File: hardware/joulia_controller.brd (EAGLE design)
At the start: 121 x 68 mm, 41 parts, among them IC1 LM2902D, IC2 LM2902D, U1 MMBT2222ALT1G, U2 MMBT2222ALT1G

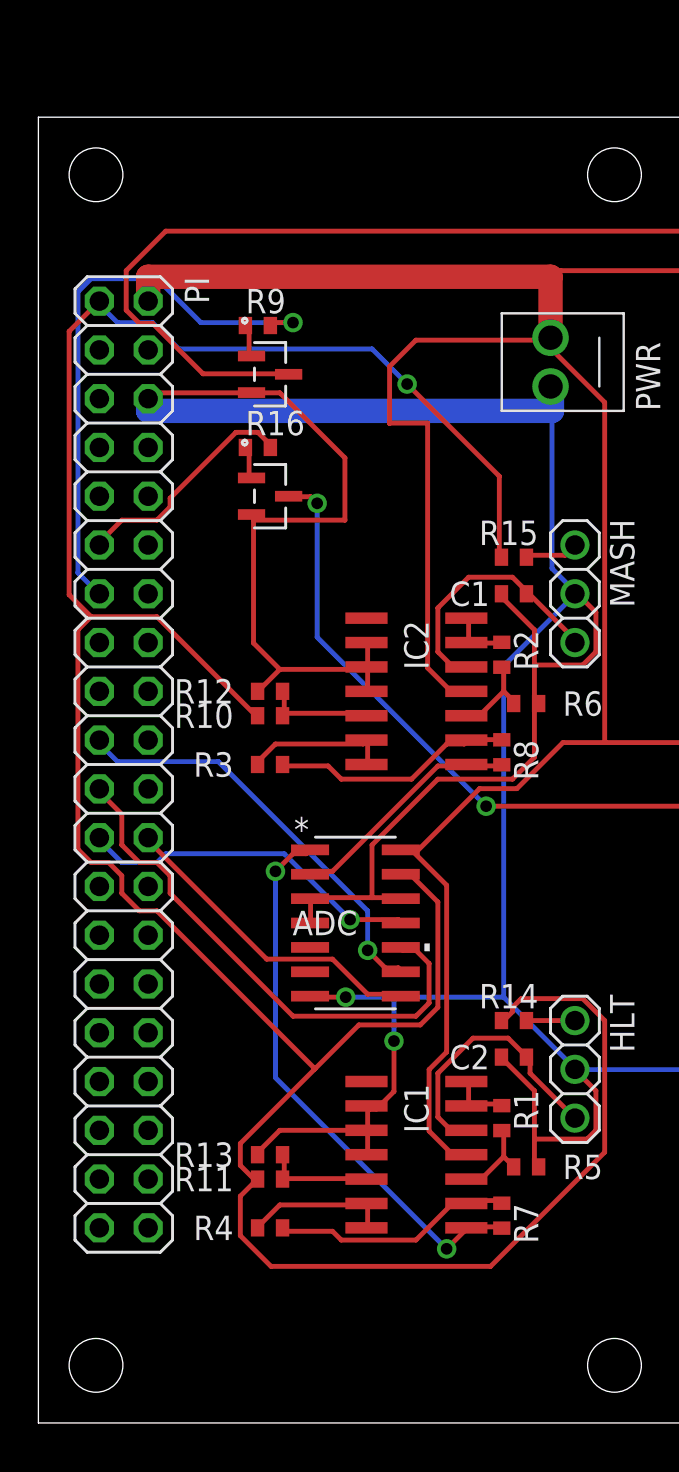
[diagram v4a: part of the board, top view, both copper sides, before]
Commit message: Adding LEDs and Fan Connector
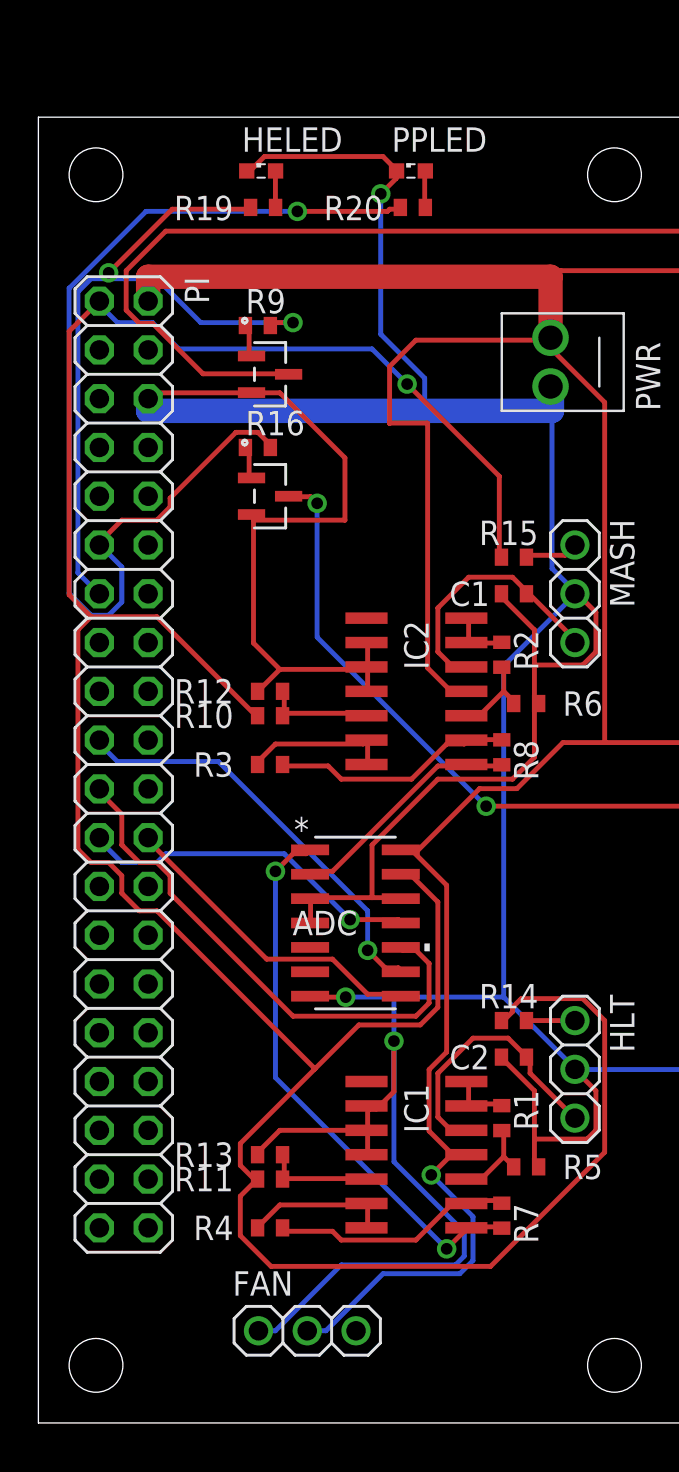
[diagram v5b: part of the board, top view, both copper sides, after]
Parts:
- added FAN: (no value), adafruit:1X03
- added HELED, PPLED: (no value), eagle-ltspice:LED_SML0603
- added R19, R20: 220, rcl:R0402
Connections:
- new net N$25: HELED.A, R19.2
- new net N$26: PPLED.A, R20.2
- net +5V: now also FAN.2
- net GND: now also FAN.1, HELED.C, PPLED.C
- net HEOUT: now also R19.1
- net PPOUT: now also R20.1
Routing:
- net GND: track 368.1 -> 415.4 mm, vias 2 -> 3
- net PPOUT: track 12.1 -> 54.0 mm, vias 0 -> 1
- net +5V: track 150.0 -> 167.7 mm, vias 0 -> 1
- net HEOUT: track 29.9 -> 39.0 mm, vias 1 -> 2
- net N$26: track 0.00 -> 1.93 mm
- net N$25: track 0.00 -> 1.90 mm
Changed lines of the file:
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@@
 <attribute name="NAME" x="37.53" y="33.07" size="1.27" layer="25" align="bottom-right"/>
 </element>
+<element name="HELED" library="eagle-ltspice" library_urn="urn:adsk.eagle:library:217" package="LED_SML0603" value="" x="11.6" y="65.2">
+<attribute name="SPICEMODEL" value="NONE" x="11.6" y="65.2" size="1.778" layer="27" display="off"/>
+<attribute name="SPICEPREFIX" value="D" x="11.6" y="65.2" size="1.778" layer="27" display="off"/>
+<attribute name="SPICETYPE" value="diode" x="11.6" y="65.2" size="1.778" layer="27" display="off"/>
+</element>
+<element name="PPLED" library="eagle-ltspice" library_urn="urn:adsk.eagle:library:217" package="LED_SML0603" value="" x="19.4" y="65.2">
+<attribute name="SPICEMODEL" value="NONE" x="19.4" y="65.2" size="1.778" layer="27" display="off"/>
+<attribute name="SPICEPREFIX" value="D" x="19.4" y="65.2" size="1.778" layer="27" display="off"/>
+<attribute name="SPICETYPE" value="diode" x="19.4" y="65.2" size="1.778" layer="27" display="off"/>
+</element>
+<element name="R19" library="rcl" library_urn="urn:adsk.eagle:library:334" package="R0402" value="220" x="11.7" y="63.3" smashed="yes">
+<attribute name="NAME" x="7.065" y="62.635" size="1.27" layer="25"/>
+</element>
+<element name="R20" library="rcl" library_urn="urn:adsk.eagle:library:334" package="R0402" value="220" x="19.5" y="63.3" smashed="yes">
+<attribute name="NAME" x="14.865" y="62.635" size="1.27" layer="25"/>
+</element>
+<element name="FAN" library="adafruit" package="1X03" value="" x="14" y="4.8"/>
 </elements>
 <signals>
@@
 <wire x1="26.67" y1="53.975" x2="26.7462" y2="53.975" width="1.27" layer="16"/>
 <wire x1="26.7462" y1="53.975" x2="26.7462" y2="52.705" width="1.27" layer="16"/>
-<wire x1="26.7462" y1="52.705" x2="5.715" y2="52.705" width="1.27" layer="16"/>
+<wire x1="26.7462" y1="52.705" x2="20.1168" y2="52.705" width="1.27" layer="16"/>
+<wire x1="20.1168" y1="52.705" x2="5.715" y2="52.705" width="1.27" layer="16"/>
 <wire x1="5.715" y1="52.705" x2="5.715" y2="53.34" width="1.27" layer="16"/>
 <wire x1="15.9639" y1="47.0154" x2="15.9639" y2="50.2539" width="0.254" layer="1"/>
@@
 <wire x1="113.5" y1="39.1" x2="113.5" y2="15.202" width="0.254" layer="1"/>
 <wire x1="113.5" y1="15.202" x2="108.2421" y2="10.8441" width="0.254" layer="1"/>
+<contactref element="HELED" pad="C"/>
+<contactref element="PPLED" pad="C"/>
+<wire x1="11.0871" y1="65.2653" x2="10.8585" y2="65.2653" width="0.254" layer="1"/>
+<wire x1="11.7729" y1="65.9511" x2="11.0871" y2="65.2653" width="0.254" layer="1"/>
+<wire x1="17.9451" y1="65.9511" x2="11.7729" y2="65.9511" width="0.254" layer="1"/>
+<wire x1="18.6309" y1="65.2653" x2="17.9451" y2="65.9511" width="0.254" layer="1"/>
+<wire x1="10.8585" y1="65.2653" x2="10.85" y2="65.2" width="0.254" layer="1"/>
+<wire x1="18.6309" y1="65.2653" x2="18.65" y2="65.2" width="0.254" layer="1"/>
+<wire x1="18.6309" y1="64.8081" x2="18.6309" y2="65.151" width="0.254" layer="1"/>
+<wire x1="17.8308" y1="64.008" x2="18.6309" y2="64.8081" width="0.254" layer="1"/>
+<wire x1="17.8308" y1="56.6928" x2="17.8308" y2="64.008" width="0.254" layer="16"/>
+<wire x1="20.1168" y1="54.4068" x2="17.8308" y2="56.6928" width="0.254" layer="16"/>
+<wire x1="20.1168" y1="52.705" x2="20.1168" y2="54.4068" width="0.254" layer="16"/>
+<wire x1="18.6309" y1="65.151" x2="18.65" y2="65.2" width="0.254" layer="1"/>
+<via x="17.8308" y="64.008" extent="1-16" drill="0.6096"/>
+<contactref element="FAN" pad="1"/>
+<wire x1="12.3444" y1="4.8006" x2="11.5443" y2="4.8006" width="0.254" layer="16"/>
+<wire x1="15.7734" y1="8.2296" x2="12.3444" y2="4.8006" width="0.254" layer="16"/>
+<wire x1="21.717" y1="8.2296" x2="15.7734" y2="8.2296" width="0.254" layer="16"/>
+<wire x1="22.1742" y1="8.6868" x2="21.717" y2="8.2296" width="0.254" layer="16"/>
+<wire x1="22.1742" y1="9.9441" x2="22.1742" y2="8.6868" width="0.254" layer="16"/>
+<wire x1="18.5166" y1="13.6017" x2="22.1742" y2="9.9441" width="0.254" layer="16"/>
+<wire x1="18.5166" y1="19.8882" x2="18.5166" y2="13.6017" width="0.254" layer="16"/>
+<wire x1="11.5443" y1="4.8006" x2="11.46" y2="4.8" width="0.254" layer="16"/>
 </signal>
 <signal name="N$4">
@@
 <wire x1="29.4894" y1="35.433" x2="29.4894" y2="53.1495" width="0.254" layer="1"/>
 <wire x1="26.7462" y1="55.8927" x2="26.67" y2="56.515" width="0.254" layer="1"/>
+<contactref element="FAN" pad="2"/>
+<wire x1="14.9733" y1="4.8006" x2="14.0589" y2="4.8006" width="0.254" layer="16"/>
+<wire x1="17.9451" y1="7.7724" x2="14.9733" y2="4.8006" width="0.254" layer="16"/>
+<wire x1="21.9456" y1="7.7724" x2="17.9451" y2="7.7724" width="0.254" layer="16"/>
+<wire x1="22.6314" y1="8.4582" x2="21.9456" y2="7.7724" width="0.254" layer="16"/>
+<wire x1="22.6314" y1="10.7442" x2="22.6314" y2="8.4582" width="0.254" layer="16"/>
+<wire x1="20.4597" y1="12.9159" x2="22.6314" y2="10.7442" width="0.254" layer="16"/>
+<wire x1="21.4884" y1="13.9446" x2="20.4597" y2="12.9159" width="0.254" layer="1"/>
+<wire x1="14.0589" y1="4.8006" x2="14" y2="4.8" width="0.254" layer="16"/>
+<wire x1="21.4884" y1="13.9446" x2="22.285" y2="13.97" width="0.254" layer="1"/>
+<via x="20.4597" y="12.9159" extent="1-16" drill="0.6096"/>
 </signal>
 <signal name="+3V3">
@@
 <wire x1="8.4582" y1="57.3024" x2="13.2588" y2="57.3024" width="0.254" layer="16"/>
 <wire x1="6.1722" y1="59.5884" x2="8.4582" y2="57.3024" width="0.254" layer="16"/>
-<wire x1="2.7432" y1="59.5884" x2="6.1722" y2="59.5884" width="0.254" layer="16"/>
+<wire x1="2.7432" y1="59.5884" x2="3.6576" y2="59.5884" width="0.254" layer="16"/>
+<wire x1="3.6576" y1="59.5884" x2="6.1722" y2="59.5884" width="0.254" layer="16"/>
 <wire x1="2.0574" y1="58.9026" x2="2.7432" y2="59.5884" width="0.254" layer="16"/>
 <wire x1="2.0574" y1="44.2722" x2="2.0574" y2="58.9026" width="0.254" layer="16"/>
@@
 <wire x1="2.9718" y1="43.3578" x2="3.175" y2="43.18" width="0.254" layer="16"/>
 <via x="13.2588" y="57.3024" extent="1-16" drill="0.6096"/>
+<contactref element="R19" pad="1"/>
+<wire x1="6.9723" y1="63.2079" x2="10.9728" y2="63.2079" width="0.254" layer="1"/>
+<wire x1="3.6576" y1="59.8932" x2="6.9723" y2="63.2079" width="0.254" layer="1"/>
+<wire x1="3.6576" y1="59.5884" x2="3.6576" y2="59.8932" width="0.254" layer="16"/>
+<wire x1="10.9728" y1="63.2079" x2="11.05" y2="63.3" width="0.254" layer="1"/>
+<via x="3.6576" y="59.8932" extent="1-16" drill="0.6096"/>
 </signal>
 <signal name="PPOUT">
@@
 <wire x1="11.8872" y1="50.9016" x2="12.08" y2="50.8" width="0.254" layer="1"/>
 <wire x1="3.2004" y1="45.8724" x2="3.175" y2="45.72" width="0.254" layer="1"/>
+<contactref element="R20" pad="1"/>
+<wire x1="18.288" y1="63.2079" x2="18.7452" y2="63.2079" width="0.254" layer="1"/>
+<wire x1="18.1737" y1="63.0936" x2="18.288" y2="63.2079" width="0.254" layer="1"/>
+<wire x1="13.4874" y1="63.0936" x2="18.1737" y2="63.0936" width="0.254" layer="1"/>
+<wire x1="5.6007" y1="63.0936" x2="13.4874" y2="63.0936" width="0.254" layer="16"/>
+<wire x1="1.6002" y1="59.0931" x2="5.6007" y2="63.0936" width="0.254" layer="16"/>
+<wire x1="1.6002" y1="43.2054" x2="1.6002" y2="59.0931" width="0.254" layer="16"/>
+<wire x1="2.7432" y1="42.0624" x2="1.6002" y2="43.2054" width="0.254" layer="16"/>
+<wire x1="3.6576" y1="42.0624" x2="2.7432" y2="42.0624" width="0.254" layer="16"/>
+<wire x1="4.3434" y1="42.7482" x2="3.6576" y2="42.0624" width="0.254" layer="16"/>
+<wire x1="4.3434" y1="44.577" x2="4.3434" y2="42.7482" width="0.254" layer="16"/>
+<wire x1="3.2004" y1="45.72" x2="4.3434" y2="44.577" width="0.254" layer="16"/>
+<wire x1="18.7452" y1="63.2079" x2="18.85" y2="63.3" width="0.254" layer="1"/>
+<wire x1="3.2004" y1="45.72" x2="3.175" y2="45.72" width="0.254" layer="16"/>
+<via x="13.4874" y="63.0936" extent="1-16" drill="0.6096"/>
 </signal>
 <signal name="N$15">
@@
 <wire x1="100.6983" y1="16.002" x2="100.665" y2="16.3" width="0.762" layer="1"/>
 </signal>
+<signal name="N$25">
+<contactref element="HELED" pad="A"/>
+<contactref element="R19" pad="2"/>
+<wire x1="12.3444" y1="63.3222" x2="12.3444" y2="65.151" width="0.254" layer="1"/>
+<wire x1="12.3444" y1="65.151" x2="12.35" y2="65.2" width="0.254" layer="1"/>
+<wire x1="12.3444" y1="63.3222" x2="12.35" y2="63.3" width="0.254" layer="1"/>
+</signal>
+<signal name="N$26">
+<contactref element="R20" pad="2"/>
+<contactref element="PPLED" pad="A"/>
+<wire x1="20.1168" y1="63.3222" x2="20.1168" y2="65.151" width="0.254" layer="1"/>
+<wire x1="20.1168" y1="65.151" x2="20.15" y2="65.2" width="0.254" layer="1"/>
+<wire x1="20.1168" y1="63.3222" x2="20.15" y2="63.3" width="0.254" layer="1"/>
+</signal>
 </signals>

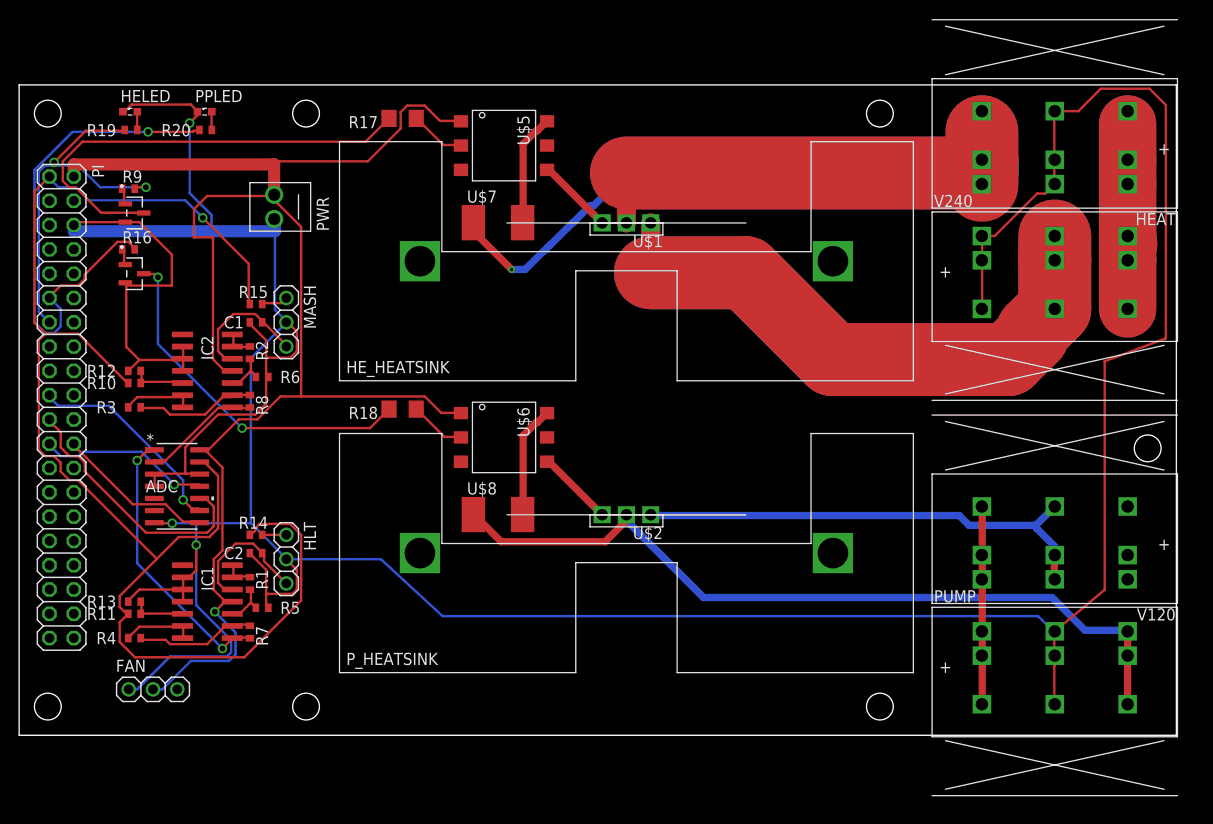
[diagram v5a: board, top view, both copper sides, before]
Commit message: Switching to mechanical relay for pump and horizontal heatsink.
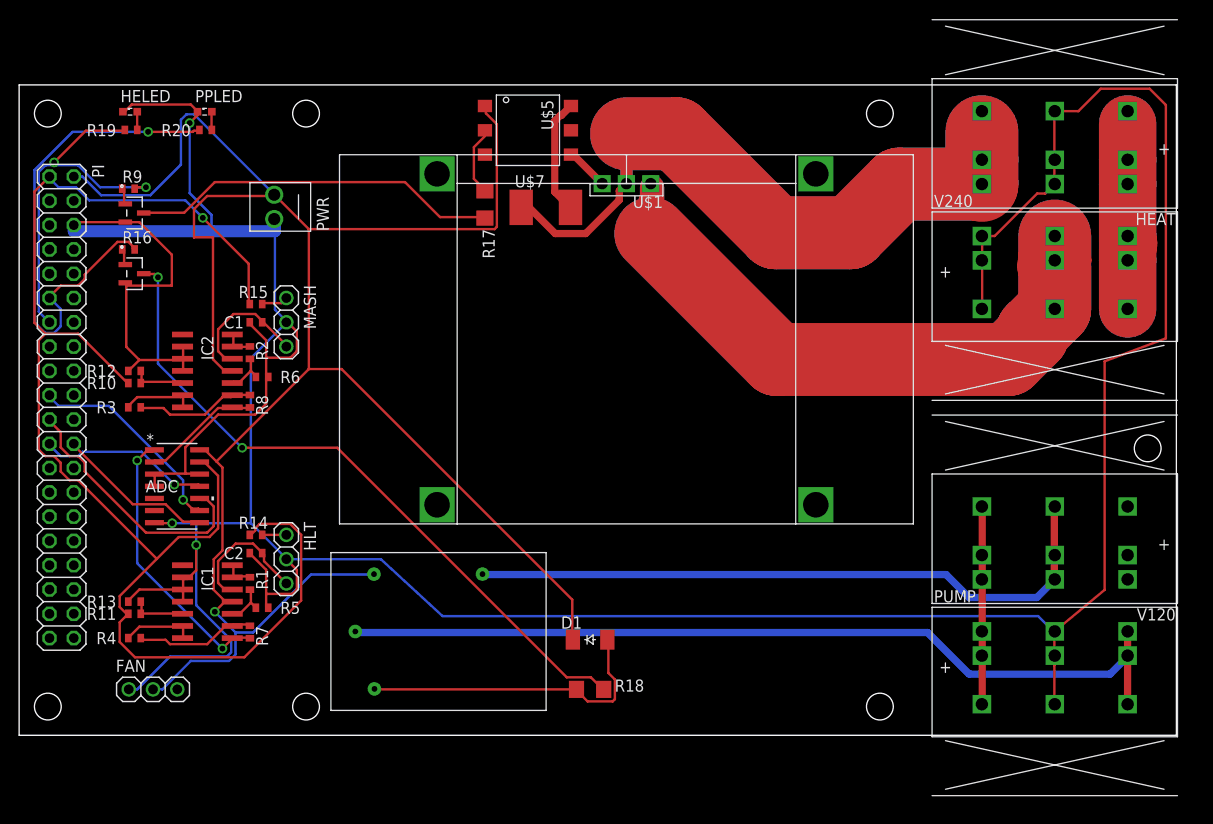
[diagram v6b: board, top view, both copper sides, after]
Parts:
- removed HE_HEATSINK, P_HEATSINK: VM1-038-1AE, digikey:VM1-038-1AE
- removed U$6: MOC3020S, digikey:6-SMD
- removed U$8: CRM2512, digikey:2512(6432METRIC)
- added D1: CGRM4001-G, diode:SOD-123_MINI-SMA
- added U$3: G5LE-1A4_DC5, digikey:G5LE-1A4_DC5
- U$2: value T3050H-6I -> VM1-038-1AEHORIZONTAL; device digikey:TO-220 -> digikey:VM2-038-1AE
- moved U$2 48.1 mm to (33.5, 60.7), turned to 0 degrees
- moved R18 35.3 mm to (59.7, 4.80), turned to 180 degrees
- moved R17 12.4 mm to (48.7, 55.5), turned to 90 degrees
- moved U$7 5.25 mm to (55.1, 55.2)
- moved U$1 4.10 mm to (63.5, 57.7)
- moved U$5 2.97 mm to (53.2, 63.3)
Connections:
- removed net N$21: U$6.P$1, U$8.P$1
- removed net N$23: U$2.G, U$6.P$3
- net +5V: now also D1.C, U$3.P$4; no longer U$6.P$6
- net 120H: now also U$3.P$1; no longer U$2.A1
- net N$17: now also D1.A, U$3.P$2; no longer U$6.P$5
- net N$24: now also U$3.P$3; no longer U$2.A2, U$8.P$2
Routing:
- net +5V: track 167.7 -> 222.5 mm
- net N$18: track 37.3 -> 71.4 mm
- net N$17: track 5.92 -> 32.4 mm
- net 120H: track 50.0 -> 69.3 mm
- net N$21: track 11.8 -> 0.00 mm
- net N$13: track 47.9 -> 38.6 mm
- net N$23: track 8.06 -> 0.00 mm
- net N$24: track 84.3 -> 91.2 mm
- net -120: track 122.9 -> 127.2 mm
- net N$19: track 8.06 -> 4.52 mm
- net N$22: track 125.6 -> 128.6 mm, vias 1 -> 0
- net N$14: track 5.87 -> 7.28 mm
